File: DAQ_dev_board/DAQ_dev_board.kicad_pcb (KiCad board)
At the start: 2 copper layers, 26 parts, among them J2 A0, A1, J3 GPIO1, GPIO2, J4 CS, DRDY, J5 SCLK, DIN, J6 DOUT, START, J7 RESET, PDWN, U2 AD8495 (TC AMP)

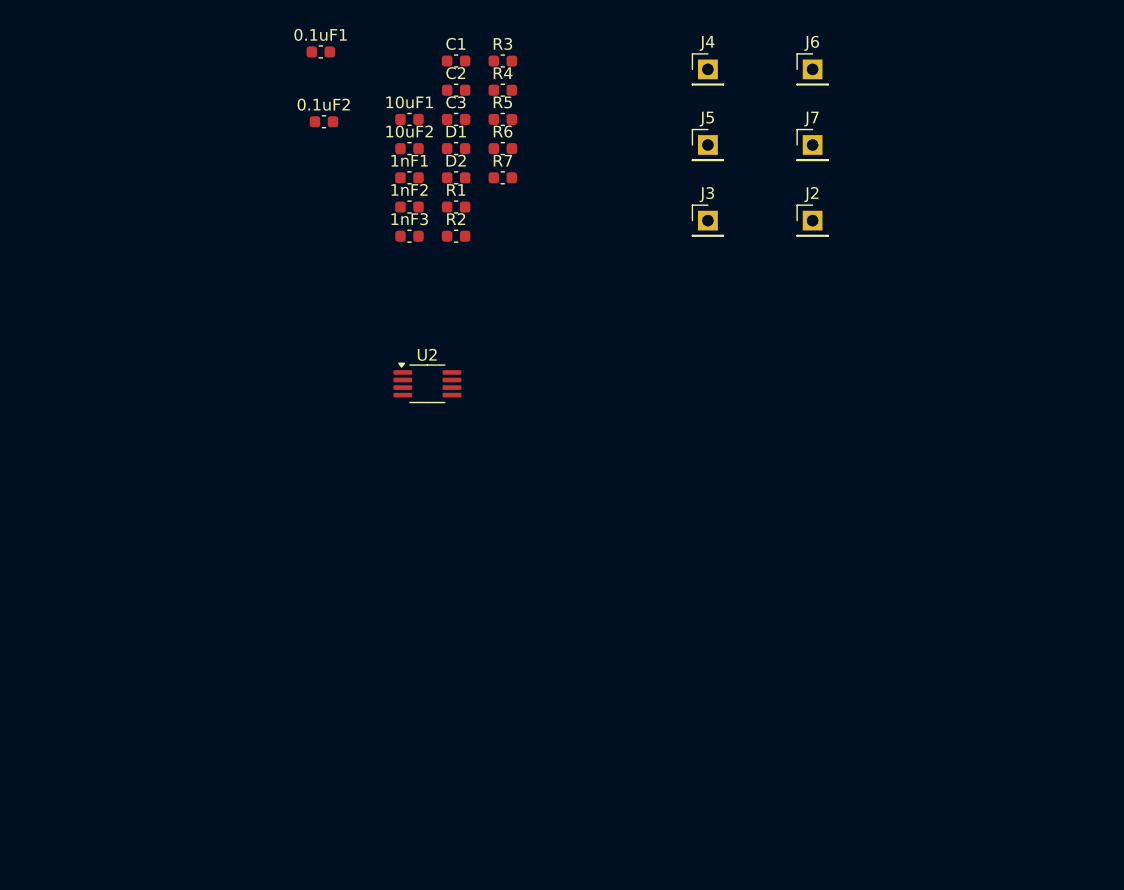
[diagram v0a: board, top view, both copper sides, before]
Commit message: updated daq board routing
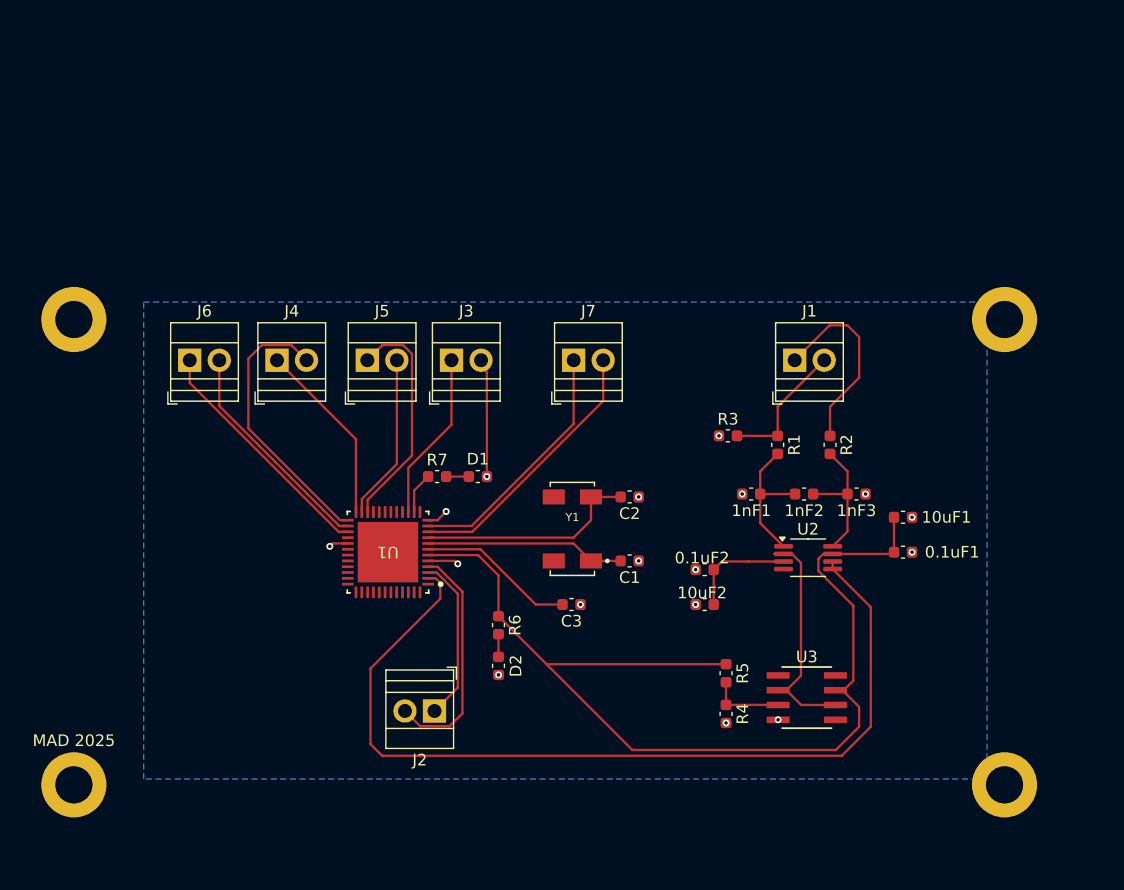
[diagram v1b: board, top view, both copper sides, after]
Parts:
- added J1: Thermocouple, TerminalBlock:TerminalBlock_Xinya_XY308-2.54-2P_1x02_P2.54mm_Horizontal, F.Cu at (167.0, 78.5)
- added MAD 2025: M3, MountingHole:MountingHole_3.2mm_M3_DIN965_Pad, F.Cu at (105.0, 115.0)
- added REF**: M3, MountingHole:MountingHole_3.2mm_M3_DIN965_Pad, F.Cu at (105.0, 75.0)
- added REF**: M3, MountingHole:MountingHole_3.2mm_M3_DIN965_Pad, F.Cu at (185.0, 75.0)
- added REF**: M3, MountingHole:MountingHole_3.2mm_M3_DIN965_Pad, F.Cu at (185.0, 115.0)
- added U1: ADS1158IRTCR (ADC), ul_ADS1158IRTCR:RTC0048A-IPC_A, F.Cu at (132.0, 95.0)
- added U3: OP777ARZ (OP AMP), ul_ADS1158IRTCR:R_8_ADI, F.Cu at (168.0, 107.5)
- added Y1: 32.768kHz, ul_ADS1158IRTCR:XTAL_ABS25-32.768KHZ-6-1-T, F.Cu at (147.9, 93.0)
- 0.1uF1: value C -> C5
- 0.1uF2: value C -> C6
- 10uF1: value C -> C4
- 10uF2: value C -> C7
- 1nF1: value C -> C3
- 1nF2: value C -> C2
- 1nF3: value C -> C1
- J2, J5, J7: footprint Connector_PinHeader_2.54mm:PinHeader_1x01_P2.54mm_Vertical -> TerminalBlock:TerminalBlock_Xinya_XY308-2.54-2P_1x02_P2.54mm_Horizontal
- J3: value GPIO1, GPIO2 -> GPIO1; footprint Connector_PinHeader_2.54mm:PinHeader_1x01_P2.54mm_Vertical -> TerminalBlock:TerminalBlock_Xinya_XY308-2.54-2P_1x02_P2.54mm_Horizontal
- J4: value CS, DRDY -> DOUT, DRDY; footprint Connector_PinHeader_2.54mm:PinHeader_1x01_P2.54mm_Vertical -> TerminalBlock:TerminalBlock_Xinya_XY308-2.54-2P_1x02_P2.54mm_Horizontal
- J6: value DOUT, START -> START, CS; footprint Connector_PinHeader_2.54mm:PinHeader_1x01_P2.54mm_Vertical -> TerminalBlock:TerminalBlock_Xinya_XY308-2.54-2P_1x02_P2.54mm_Horizontal
- moved 0.1uF1 66.0 mm to (176.3, 95.0), turned to 180 degrees
- moved J6 59.1 mm to (115.0, 78.5)
- moved R4 56.9 mm to (161.1, 108.9), turned to -90 degrees
- moved 10uF1 54.5 mm to (176.3, 92.0), turned to 180 degrees
- moved J2 53.2 mm to (136.0, 108.7), turned to 180 degrees
- moved R5 51.3 mm to (161.1, 105.4), turned to -90 degrees
- moved 0.1uF2 50.5 mm to (159.2, 96.5)
- moved 10uF2 46.7 mm to (159.2, 99.5)
- moved C1 45.5 mm to (152.8, 95.8), turned to 180 degrees
- moved J4 44.7 mm to (122.5, 78.5)
- moved 1nF3 44.4 mm to (172.3, 90.0), turned to 180 degrees
- moved C3 42.9 mm to (147.8, 99.5), turned to 180 degrees
- moved D2 42.1 mm to (141.5, 104.8), turned to 90 degrees
- moved 1nF2 41.9 mm to (167.8, 90.0), turned to 180 degrees
- moved R6 41.0 mm to (141.5, 101.3), turned to -90 degrees
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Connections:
- D1 pad 1: Net-(D1-K) -> GND
- R7 pad 1: Net-(D1-K) -> Net-(U1-GPIO0)
- R7 pad 2: GND -> Net-(D1-A)
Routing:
- net +5V: track 0.00 -> 90.0 mm
- net TC_CHIP_OUT: track 0.00 -> 77.6 mm
- net GND: track 0.00 -> 26.0 mm, vias 0 -> 17
- net Net-(J4-Pin_2): track 0.00 -> 23.8 mm
- net Net-(J7-Pin_2): track 0.00 -> 23.2 mm
- net Net-(J7-Pin_1): track 0.00 -> 21.6 mm
- net Net-(J6-Pin_1): track 0.00 -> 20.8 mm
- net Net-(J2-Pin_2): track 0.00 -> 20.2 mm
- net TC_OFFSET: track 0.00 -> 20.1 mm
- net Net-(J5-Pin_1): track 0.00 -> 19.9 mm
- net Net-(J6-Pin_2): track 0.00 -> 19.3 mm
- net Net-(U1-XTAL2): track 0.00 -> 19.2 mm
- net Net-(U1-XTAL1): track 0.00 -> 17.2 mm
- net /+: track 0.00 -> 16.7 mm
- net Net-(J4-Pin_1): track 0.00 -> 15.9 mm
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- added copper zone on B.Cu, net GND

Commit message: update
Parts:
- added J6: +5V, GND, TerminalBlock:TerminalBlock_Xinya_XY308-2.54-2P_1x02_P2.54mm_Horizontal, F.Cu at (123.8, 108.7)
- moved MAD 2025 5.00 mm to (105.0, 110.0)
- moved REF** 5.00 mm to (185.0, 110.0)
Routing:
- net GND: track 26.0 -> 30.9 mm, vias 17 -> 19

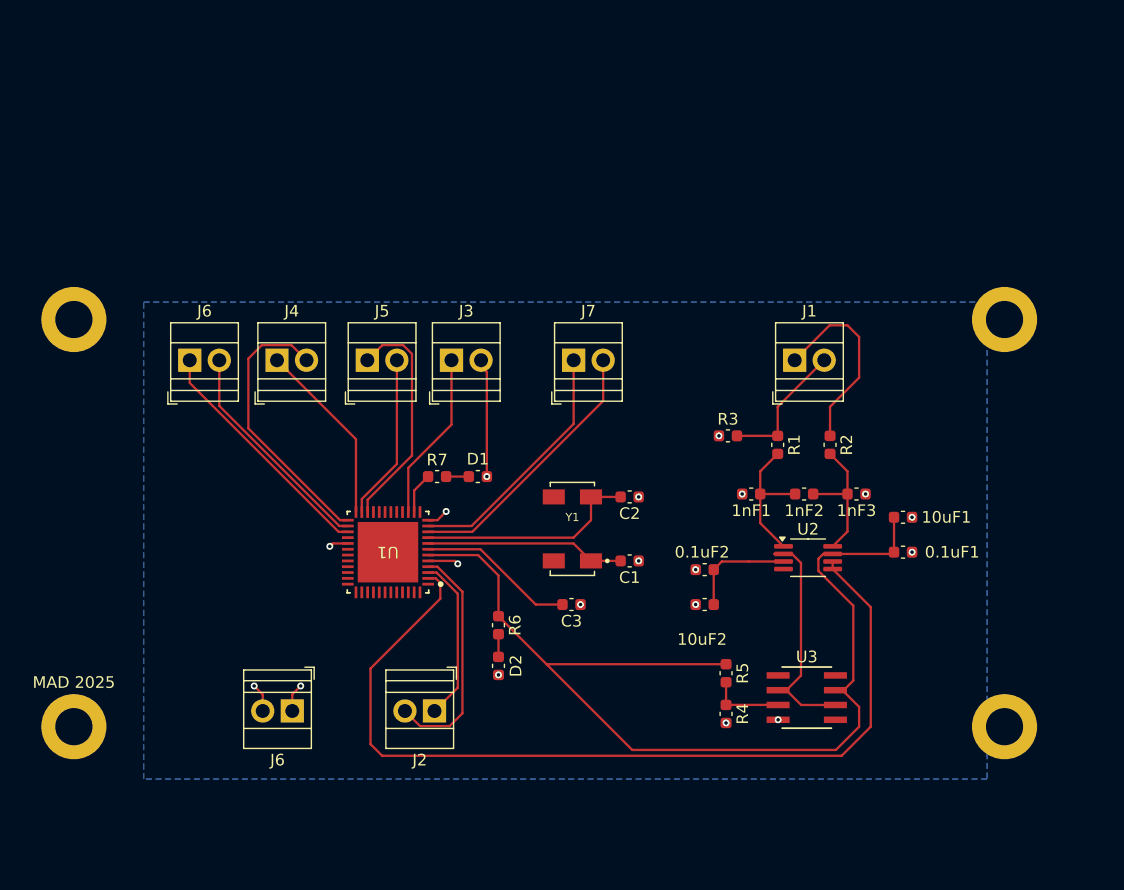
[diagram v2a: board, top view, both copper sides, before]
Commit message: updated pinout and other fixes
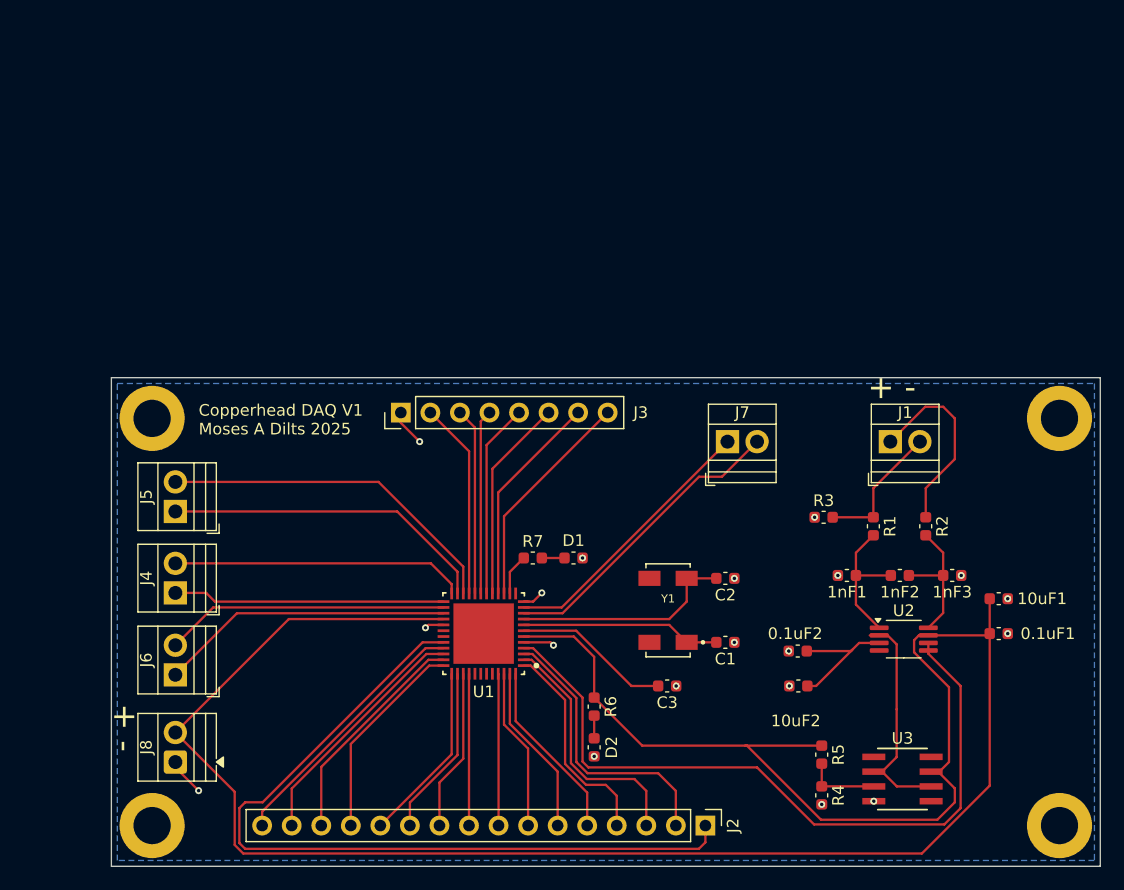
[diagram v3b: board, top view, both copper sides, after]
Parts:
- removed the J6 at (123.8, 108.7)
- added J8: GND, 5VIN, TerminalBlock:TerminalBlock_Xinya_XY308-2.54-2P_1x02_P2.54mm_Horizontal, F.Cu at (113.7, 113.0)
- J2: value A0, A1 -> Conn_01x16_Pin; footprint TerminalBlock:TerminalBlock_Xinya_XY308-2.54-2P_1x02_P2.54mm_Horizontal -> Connector_PinHeader_2.54mm:PinHeader_1x16_P2.54mm_Vertical
- J3: value GPIO1 -> Conn_01x08_Pin; footprint TerminalBlock:TerminalBlock_Xinya_XY308-2.54-2P_1x02_P2.54mm_Horizontal -> Connector_PinHeader_2.54mm:PinHeader_1x08_P2.54mm_Vertical
- moved J6 27.1 mm to (113.7, 105.5), turned to 90 degrees
- moved J2 25.3 mm to (159.3, 118.5), turned to -90 degrees
- moved J4 21.8 mm to (113.7, 98.5), turned to 90 degrees
- moved J5 21.0 mm to (113.7, 91.5), turned to 90 degrees
- moved J7 15.0 mm to (161.2, 85.5)
- moved MAD 2025 10.8 mm to (111.7, 118.5)
- moved REF** 10.8 mm to (111.7, 83.5)
- moved 0.1uF1 10.8 mm to (184.5, 102.0)
- moved 10uF1 10.8 mm to (184.5, 99.0)
- moved 1nF1 10.8 mm to (171.4, 97.0)
- moved 1nF2 10.8 mm to (176.0, 97.0)
- moved 1nF3 10.8 mm to (180.5, 97.0)
- moved C1 10.8 mm to (161.0, 102.8)
- moved C2 10.8 mm to (161.0, 97.2)
- moved C3 10.8 mm to (156.0, 106.5)
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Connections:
- J3 pad 1: Net-(J3-Pin_1) -> GND
- J3 pad 2: GND -> Net-(J3-Pin_2)
- U1 pad 1: unconnected-(U1-AIN3-Pad1) -> Net-(J2-Pin_4)
- U1 pad 15: Net-(J3-Pin_1) -> Net-(J3-Pin_8)
- U1 pad 16: unconnected-(U1-GPIO2-Pad16) -> Net-(J3-Pin_7)
- U1 pad 17: unconnected-(U1-GPIO3-Pad17) -> Net-(J3-Pin_6)
- U1 pad 18: unconnected-(U1-GPIO4-Pad18) -> Net-(J3-Pin_5)
- U1 pad 19: unconnected-(U1-GPIO5-Pad19) -> Net-(J3-Pin_4)
- U1 pad 2: TC_CHIP_OUT -> Net-(J2-Pin_3)
- U1 pad 20: unconnected-(U1-GPIO6-Pad20) -> Net-(J3-Pin_3)
- U1 pad 21: unconnected-(U1-GPIO7-Pad21) -> Net-(J3-Pin_2)
- U1 pad 22: Net-(J5-Pin_1) -> Net-(J5-Pin_2)
- U1 pad 23: Net-(J5-Pin_2) -> Net-(J5-Pin_1)
- U1 pad 24: Net-(J4-Pin_1) -> Net-(J4-Pin_2)
- U1 pad 25: Net-(J4-Pin_2) -> Net-(J4-Pin_1)
- U1 pad 3: Net-(J2-Pin_1) -> Net-(J2-Pin_2)
- U1 pad 32: unconnected-(U1-AINCOM-Pad32) -> Net-(J2-Pin_1)
- U1 pad 33: unconnected-(U1-AIN15-Pad33) -> Net-(J2-Pin_16)
- U1 pad 34: unconnected-(U1-AIN14-Pad34) -> Net-(J2-Pin_15)
- U1 pad 35: unconnected-(U1-AIN13-Pad35) -> Net-(J2-Pin_14)
- U1 pad 36: unconnected-(U1-AIN12-Pad36) -> Net-(J2-Pin_13)
- U1 pad 37: unconnected-(U1-AIN11-Pad37) -> Net-(J2-Pin_12)
- U1 pad 38: unconnected-(U1-AIN10-Pad38) -> Net-(J2-Pin_11)
- U1 pad 39: unconnected-(U1-AIN9-Pad39) -> Net-(J2-Pin_10)
- U1 pad 4: Net-(J2-Pin_2) -> TC_CHIP_OUT
- U1 pad 40: unconnected-(U1-AIN8-Pad40) -> Net-(J2-Pin_9)
- U1 pad 45: unconnected-(U1-AIN7-Pad45) -> Net-(J2-Pin_8)
- U1 pad 46: unconnected-(U1-AIN6-Pad46) -> Net-(J2-Pin_7)
- U1 pad 47: unconnected-(U1-AIN5-Pad47) -> Net-(J2-Pin_6)
- U1 pad 48: unconnected-(U1-AIN4-Pad48) -> Net-(J2-Pin_5)
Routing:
- net +5V: track 90.0 -> 199.5 mm
- net Net-(J2-Pin_1): track 14.2 -> 68.4 mm
- net Net-(J2-Pin_16): track 0.00 -> 22.6 mm
- net Net-(J2-Pin_3): track 0.00 -> 21.4 mm
- net Net-(J2-Pin_15): track 0.00 -> 21.0 mm
- net Net-(J2-Pin_14): track 0.00 -> 19.4 mm
- net Net-(J3-Pin_8): track 0.00 -> 19.2 mm
- net Net-(J2-Pin_4): track 0.00 -> 18.4 mm
- net Net-(J3-Pin_7): track 0.00 -> 18.4 mm
- net Net-(J2-Pin_13): track 0.00 -> 17.8 mm
- net Net-(J3-Pin_6): track 0.00 -> 17.5 mm
- net Net-(J3-Pin_2): track 0.00 -> 16.9 mm
- net Net-(J3-Pin_5): track 0.00 -> 16.7 mm
- net Net-(J3-Pin_3): track 0.00 -> 16.1 mm
- net Net-(J3-Pin_4): track 0.00 -> 15.9 mm
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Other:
- board outline added: 85 x 42 mm
- board text added: "+ -"
- board text added: "Copperhead DAQ V1 Moses A Dilts 2025"

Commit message: added pulldowns and replaced screw terminals with header pins
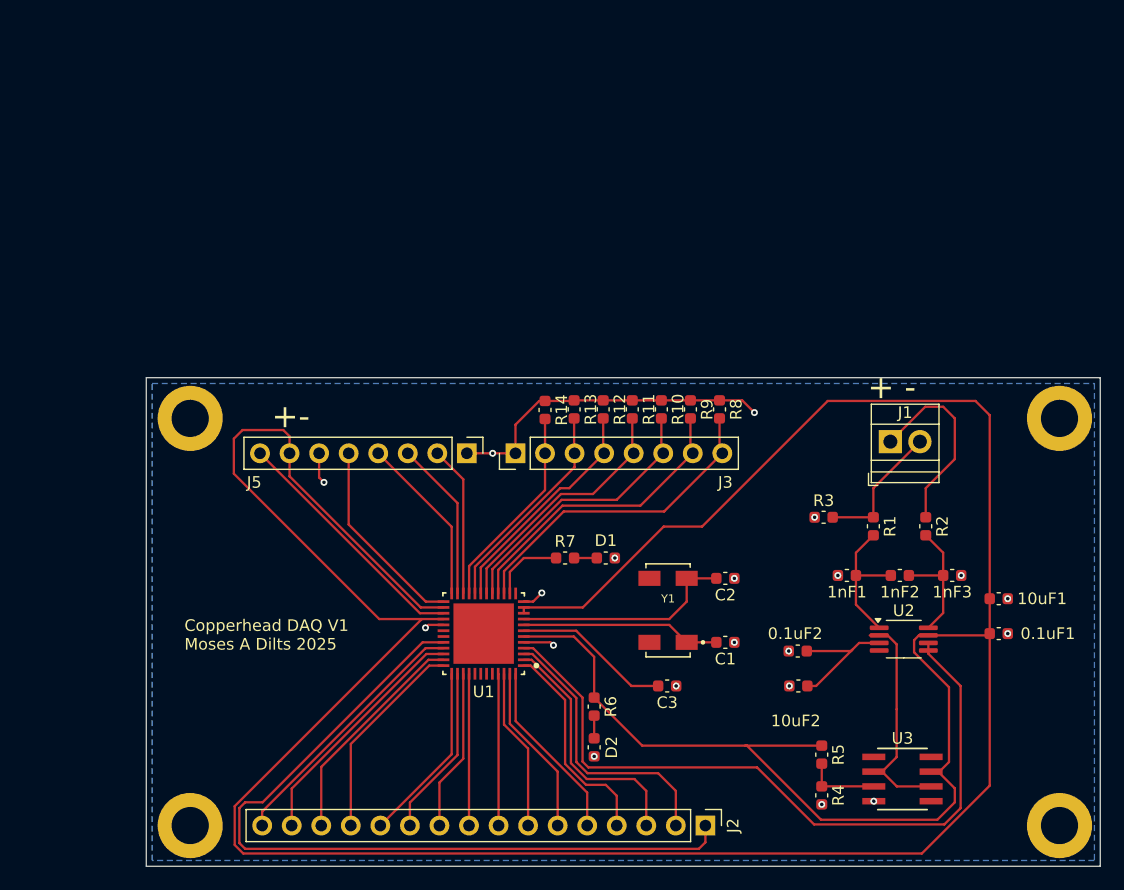
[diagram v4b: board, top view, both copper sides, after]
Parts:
- removed J4: DOUT, DRDY, TerminalBlock:TerminalBlock_Xinya_XY308-2.54-2P_1x02_P2.54mm_Horizontal
- removed J6: START, CS, TerminalBlock:TerminalBlock_Xinya_XY308-2.54-2P_1x02_P2.54mm_Horizontal
- removed J7: RESET, PDWN, TerminalBlock:TerminalBlock_Xinya_XY308-2.54-2P_1x02_P2.54mm_Horizontal
- removed J8: GND, 5VIN, TerminalBlock:TerminalBlock_Xinya_XY308-2.54-2P_1x02_P2.54mm_Horizontal
- added R10: 10k, Capacitor_SMD:C_0603_1608Metric, F.Cu at (155.5, 82.7)
- added R11: 10k, Capacitor_SMD:C_0603_1608Metric, F.Cu at (153.0, 82.7)
- added R12: 10k, Capacitor_SMD:C_0603_1608Metric, F.Cu at (150.5, 82.7)
- added R13: 10k, Capacitor_SMD:C_0603_1608Metric, F.Cu at (148.0, 82.7)
- added R14: 10k, Capacitor_SMD:C_0603_1608Metric, F.Cu at (145.5, 82.8)
- added R8: 10k, Capacitor_SMD:C_0603_1608Metric, F.Cu at (160.5, 82.7)
- added R9: 10k, Capacitor_SMD:C_0603_1608Metric, F.Cu at (158.0, 82.7)
- J5: value SCLK, DIN -> Conn_01x08_Pin; footprint TerminalBlock:TerminalBlock_Xinya_XY308-2.54-2P_1x02_P2.54mm_Horizontal -> Connector_PinHeader_2.54mm:PinHeader_1x08_P2.54mm_Vertical
- moved J5 25.5 mm to (138.8, 86.5), turned to -90 degrees
- moved J3 10.5 mm to (143.0, 86.5)
- moved MAD 2025 3.28 mm to (115.0, 118.5)
- moved REF** 3.28 mm to (115.0, 83.5)
- moved D1 2.78 mm to (150.7, 95.5)
- moved R7 2.78 mm to (147.2, 95.5)
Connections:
- J5 pad 1: Net-(J5-Pin_1) -> GND
- U1 pad 10: Net-(J7-Pin_2) -> +5V
- U1 pad 11: Net-(J7-Pin_1) -> +5V
- U1 pad 23: Net-(J5-Pin_1) -> Net-(J5-Pin_3)
- U1 pad 24: Net-(J4-Pin_2) -> Net-(J5-Pin_4)
- U1 pad 25: Net-(J4-Pin_1) -> Net-(J5-Pin_5)
- U1 pad 26: Net-(J6-Pin_2) -> +5V
- U1 pad 27: Net-(J6-Pin_1) -> Net-(J5-Pin_8)
- U1 pad 49: unconnected-(U1-EP-Pad49) -> GND
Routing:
- net +5V: track 199.5 -> 303.8 mm
- net Net-(J5-Pin_1): track 28.3 -> 0.00 mm
- net Net-(J7-Pin_2): track 26.2 -> 0.00 mm
- net Net-(J4-Pin_2): track 25.3 -> 0.00 mm
- net Net-(J6-Pin_1): track 25.2 -> 0.00 mm
- net GND: track 24.6 -> 49.3 mm, vias 19 -> 20
- net Net-(J6-Pin_2): track 24.4 -> 0.00 mm
- net Net-(J7-Pin_1): track 23.4 -> 0.00 mm
- net Net-(J4-Pin_1): track 23.4 -> 0.00 mm
- net Net-(J5-Pin_8): track 0.00 -> 21.5 mm
- net Net-(J5-Pin_2): track 30.1 -> 13.0 mm
- net Net-(J5-Pin_5): track 0.00 -> 17.0 mm
- net Net-(J5-Pin_4): track 0.00 -> 14.7 mm
- net Net-(J5-Pin_3): track 0.00 -> 13.8 mm
- net Net-(J3-Pin_8): track 19.2 -> 28.0 mm
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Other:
- board size 85 x 42 mm -> 82 x 42 mm
- board text added: "+-"
